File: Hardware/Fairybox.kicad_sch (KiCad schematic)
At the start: 71 parts, among them J1 REED, Q1 SI2302, Q10 C114, Q2 C3200, Q3 C114, Q4 C114, Q5 C3200, Q6 C114, Q7 C114, Q8 C114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

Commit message: Misc changes I forget
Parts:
- removed D8: ORNG, LED_THT:LED_D3.0mm-3, symbol Device:LED_Dual_AAK
- added D22: LED_handsolder, Diode_SMD:D_1206_3216Metric_Pad1.42x1.75mm_HandSolder, symbol Device:LED_Small_Filled
- added D23: LED_nominal, Diode_SMD:D_1206_3216Metric, symbol Device:LED_Small_Filled
- TP1: value GND -> RST
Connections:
- net B- is gone; now on net LI-ION_NEG: BAT1.2 (-), UM1.6 (B-)
- net Q1_BASE: now also R6.2; no longer R6.1
- net REED_RETURN: now also CC3.1, R6.1; no longer R6.2
- net at DI1.2 (A), DI2.2 (A): now also D22.1 (K), D23.1 (K)
- net +BATT renamed CHARGE BOARD OUT B+
- net CHARGE BOARD OUT B+: no longer CC3.1
- net -BATT renamed CHARGE BOARD OUT B-
- net B+ renamed LI-ION_NEG
- net D8_AN1 renamed D22_AN
- net D22_AN: now also D22.2 (A)
- net D8_AN2 renamed D23_AN
- net D23_AN: now also D23.2 (A)
- net RP8 renamed R7_AN
- net SPI RST: no longer names the net of R5.1, TP1.1 (Pin_1), U1.1 (RST)
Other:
- note added: "3.7 LiIon Power Input"
- note added: "5V Power Regulation"
- note added: "ATTiny85 Microcontroller"
- note added: "Ground VIAs"
- note removed: "Vf=1.91"
- moved on the sheet: BAT1, CC3, CC4, CE1, J1, Q1, R5, R6, R7, TP1, TP2, TP3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

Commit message: Misc hardware changes
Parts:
- removed CC3: 2.2nF, Capacitor_THT:C_Disc_D3.0mm_W2.0mm_P2.50mm, symbol Device:C
- removed DI1, DI2: 1N914, Diode_THT:D_DO-35_SOD27_P7.62mm_Horizontal, symbol Diode:1N914
- removed R18, R8: 4.7K, Resistor_THT:R_Axial_DIN0204_L3.6mm_D1.6mm_P5.08mm_Horizontal, symbol Device:R
- removed R19, R9: 47K, Resistor_THT:R_Axial_DIN0204_L3.6mm_D1.6mm_P5.08mm_Horizontal, symbol Device:R
- removed R6: 1K, Resistor_THT:R_Axial_DIN0204_L3.6mm_D1.6mm_P5.08mm_Horizontal, symbol Device:R
- removed R7: 300R, Resistor_THT:R_Axial_DIN0204_L3.6mm_D1.6mm_P5.08mm_Horizontal, symbol Device:R
- added D24, D9: BLUE, Diode_SMD:D_1206_3216Metric, symbol Device:LED_Small_Filled
- added D25: RED, Diode_SMD:D_1206_3216Metric, symbol Device:LED_Small_Filled
- added R16, R8, R9: ??R, Resistor_SMD:R_1206_3216Metric, symbol Device:R_Small
- added R6: 1K, Resistor_SMD:R_1206_3216Metric, symbol Device:R_Small
- CC4: value 0.1uF -> 0.22uF
- D21: renamed from D22; value LED_handsolder -> BLUE
- D23: value LED_nominal -> RED
- Q2, Q5: value C3200 -> C114
- TP10: value TestPoint_Small -> Q8_COL_TP
- TP11: value TestPoint_Small -> Q9_COL_TP
- TP12: value TestPoint_Small -> Q10_COL_TP
- TP6: value TestPoint_Small -> TPP
- TP7: value TestPoint_Small -> Q3_COL TP
- TP8: value TestPoint_Small -> Q2_TP
- TP9: value TestPoint_Small -> Q5_COL TP
- renumbered D21 to D22
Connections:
- net Q2_BASE is gone; now on net MCU GPIO4: Q2.3 (B)
- net Q5_BASE is gone; now on net MCU GPIO3: Q5.3 (B)
- net +5V: now also R16.1, R8.1, R9.1
- net D7_AN: no longer D4.1 (K), D7.2 (A)
- net LI-ION_NEG: no longer BAT1.1 (+), UM1.5 (B+)
- net Q1_BASE: now also R6.2
- net Q2_COL: now also D24.1 (K), D25.1 (K)
- net Q6_COL: now also D9.1 (K)
- net Q7_COL: now also D21.1 (K)
- net Q8_COL: now also D23.1 (K)
- net REED_RETURN: now also R6.1
- net MCU RST: now reaches R5.1, TP1.1 (Pin_1), U1.1 (RST)
- net Q3_COL renamed D6_AN
- new net: D4.1 (K), D7.2 (A)
- new net D24_AN: D24.2 (A), R8.2
- new net D25_AN: D25.2 (A), R16.2
- new net D9_AN: D9.2 (A), R9.2
- new net LI-ION_POS: BAT1.1 (+), UM1.5 (B+)
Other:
- note added: "D6 Vf=3V 5V-3V=2V/0.015A = 133Ω 2V/15Ω = .013A"
- note added: "For oscilloscope spring clips 2"
- note added: "SMD LED"
- note added: "SMD resistor"
- note added: "Test point grounds"
- note removed: "(5-1.91)/470 = 20mA green + 8mA red = orange"
- note removed: "D8 illuminates when either QN9 or QN10 light. The diodes stop D20 and D21 from sinking their current to the transistor collectors opposite of them."
- note removed: "De-ring reed switch"
- note removed: "Poor man's and gate"
- note removed: "Vd=0.461"
- note removed: "Vd=0.462"
- note removed: "Vf=2.05"
- note removed: "Vf=3.06 Ic=0.019A"
- moved on the sheet: CC4, D1, D18, D19, D2, D20, D21, D22, D23, D3, D4, D5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

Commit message: Updated testpoints and silkscreen
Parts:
- JP2, JP4, JP6, JP7, JP8: footprint UltraLibrary:Via-GND -> UltraLibrary:PTH-Test_Point; symbol ultra_library:ViaGND -> ultra_library:PTH-TestPoint_to_GND
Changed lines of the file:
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@@
     (effects (font (size 1 1)) (justify left bottom))
   )
-  (symbol (lib_id "ultra_library:ViaGND") (at 256.54 250.825 0) (unit 1)
+  (symbol (lib_id "ultra_library:PTH-TestPoint_to_GND") (at 256.54 250.825 0) (unit 1)
     (in_bom yes) (on_board yes)
     (property "Reference" "JP7" (id 0) (at 254 248.285 0)
@@
       (effects (font (size 1.27 1.27)) (justify left) hide)
     )
-    (property "Footprint" "UltraLibrary:Via-GND" (id 2) (at 256.54 250.825 0)
+    (property "Footprint" "UltraLibrary:PTH-Test_Point" (id 2) (at 256.54 250.825 0)
       (effects (font (size 1.27 1.27)) hide)
     )
@@
     (pin "2")
   )
-  (symbol (lib_id "ultra_library:ViaGND") (at 251.46 250.825 0) (unit 1)
+  (symbol (lib_id "ultra_library:PTH-TestPoint_to_GND") (at 251.46 250.825 0) (unit 1)
     (in_bom yes) (on_board yes)
     (property "Reference" "JP8" (id 0) (at 248.92 248.285 0)
@@
       (effects (font (size 1.27 1.27)) (justify left) hide)
     )
-    (property "Footprint" "UltraLibrary:Via-GND" (id 2) (at 251.46 250.825 0)
+    (property "Footprint" "UltraLibrary:PTH-Test_Point" (id 2) (at 251.46 250.825 0)
       (effects (font (size 1.27 1.27)) hide)
     )
@@
     (pin "1")
   )
-  (symbol (lib_id "ultra_library:ViaGND") (at 245.11 250.825 0) (unit 1)
+  (symbol (lib_id "ultra_library:PTH-TestPoint_to_GND") (at 245.11 250.825 0) (unit 1)
     (in_bom yes) (on_board yes)
     (property "Reference" "JP6" (id 0) (at 242.57 248.285 0)
@@
       (effects (font (size 1.27 1.27)) (justify left) hide)
     )
-    (property "Footprint" "UltraLibrary:Via-GND" (id 2) (at 245.11 250.825 0)
+    (property "Footprint" "UltraLibrary:PTH-Test_Point" (id 2) (at 245.11 250.825 0)
       (effects (font (size 1.27 1.27)) hide)
     )
@@
     (pin "2")
   )
-  (symbol (lib_id "ultra_library:ViaGND") (at 262.255 250.825 0) (unit 1)
+  (symbol (lib_id "ultra_library:PTH-TestPoint_to_GND") (at 262.255 250.825 0) (unit 1)
     (in_bom yes) (on_board yes)
     (property "Reference" "JP4" (id 0) (at 259.715 248.285 0)
@@
       (effects (font (size 1.27 1.27)) (justify left) hide)
     )
-    (property "Footprint" "UltraLibrary:Via-GND" (id 2) (at 262.255 250.825 0)
+    (property "Footprint" "UltraLibrary:PTH-Test_Point" (id 2) (at 262.255 250.825 0)
       (effects (font (size 1.27 1.27)) hide)
     )
@@
     (pin "1")
   )
-  (symbol (lib_id "ultra_library:ViaGND") (at 239.395 250.825 0) (unit 1)
+  (symbol (lib_id "ultra_library:PTH-TestPoint_to_GND") (at 239.395 250.825 0) (unit 1)
     (in_bom yes) (on_board yes)
     (property "Reference" "JP2" (id 0) (at 236.855 248.285 0)
@@
       (effects (font (size 1.27 1.27)) (justify left) hide)
     )
-    (property "Footprint" "UltraLibrary:Via-GND" (id 2) (at 239.395 250.825 0)
+    (property "Footprint" "UltraLibrary:PTH-Test_Point" (id 2) (at 239.395 250.825 0)
       (effects (font (size 1.27 1.27)) hide)
     )
@@
     )
     (path "/d32c4ef7-dff3-42ca-b263-850b4f362096"
-      (reference "JP2") (unit 1) (value "ViaGND") (footprint "UltraLibrary:Via-GND")
+      (reference "JP2") (unit 1) (value "ViaGND") (footprint "UltraLibrary:PTH-Test_Point")
     )
     (path "/5a3db8f0-f842-4403-92aa-21d7fe3462d6"
@@
     )
     (path "/cfccbb7b-ccad-4118-94a3-53227b3d839f"
-      (reference "JP4") (unit 1) (value "ViaGND") (footprint "UltraLibrary:Via-GND")
+      (reference "JP4") (unit 1) (value "ViaGND") (footprint "UltraLibrary:PTH-Test_Point")
     )
     (path "/73116c89-7ad9-480c-9a9b-9373298241f3"
@@
     )
     (path "/4da5f2d2-051f-4fbb-b355-53557e1b2b87"
-      (reference "JP6") (unit 1) (value "ViaGND") (footprint "UltraLibrary:Via-GND")
+      (reference "JP6") (unit 1) (value "ViaGND") (footprint "UltraLibrary:PTH-Test_Point")
     )
     (path "/02ec95bc-9b18-4028-a83d-b583d5fdd405"
-      (reference "JP7") (unit 1) (value "ViaGND") (footprint "UltraLibrary:Via-GND")
+      (reference "JP7") (unit 1) (value "ViaGND") (footprint "UltraLibrary:PTH-Test_Point")
     )
     (path "/111b3249-5eff-4101-9c94-370558af5ec1"
-      (reference "JP8") (unit 1) (value "ViaGND") (footprint "UltraLibrary:Via-GND")
+      (reference "JP8") (unit 1) (value "ViaGND") (footprint "UltraLibrary:PTH-Test_Point")
     )
     (path "/36b807a0-a817-4a09-a5f8-3ee2792c5a71"

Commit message: misc
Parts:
- added D?: D_Schottky, symbol Device:D_Schottky
- added R?: 22R, Resistor_THT:R_Axial_DIN0204_L3.6mm_D1.6mm_P5.08mm_Horizontal, symbol Device:R
- added R? (x5): 250R, Resistor_THT:R_Axial_DIN0204_L3.6mm_D1.6mm_P5.08mm_Horizontal, symbol Device:R
- R16: value ??R -> 170R
- R8: value ??R -> 470R
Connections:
- net +5V: now also D?.2 (A); no longer CC4.1, TP5.1 (Pin_1), U1.8 (VCC)
- net MCU GPIO0 MOSI: now also R?.2
- net MCU GPIO1 MISO: now also R?.2
- net MCU GPIO2 SCK: now also R?.2
- net MCU GPIO3: now also R?.2
- net MCU GPIO4: now also R?.2
- new net: R?.2, TP5.1 (Pin_1)
- new net: CC4.1, R?.1, U1.8 (VCC)
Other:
- note added: "1/8W Current limiting resistors GPIO Imax=20mA 4.5V/0.020A = 0.018A Also protects ISP programmer"
- note added: "1W current limiting resistor 5V/22 = 0.230A Also prevents ISP from powering LEDs."
- note added: "BLUE"
- note added: "RED"
- moved on the sheet: D3, D4, D7, Q4, Q5, R3, R4, TP5, TP6, TP9

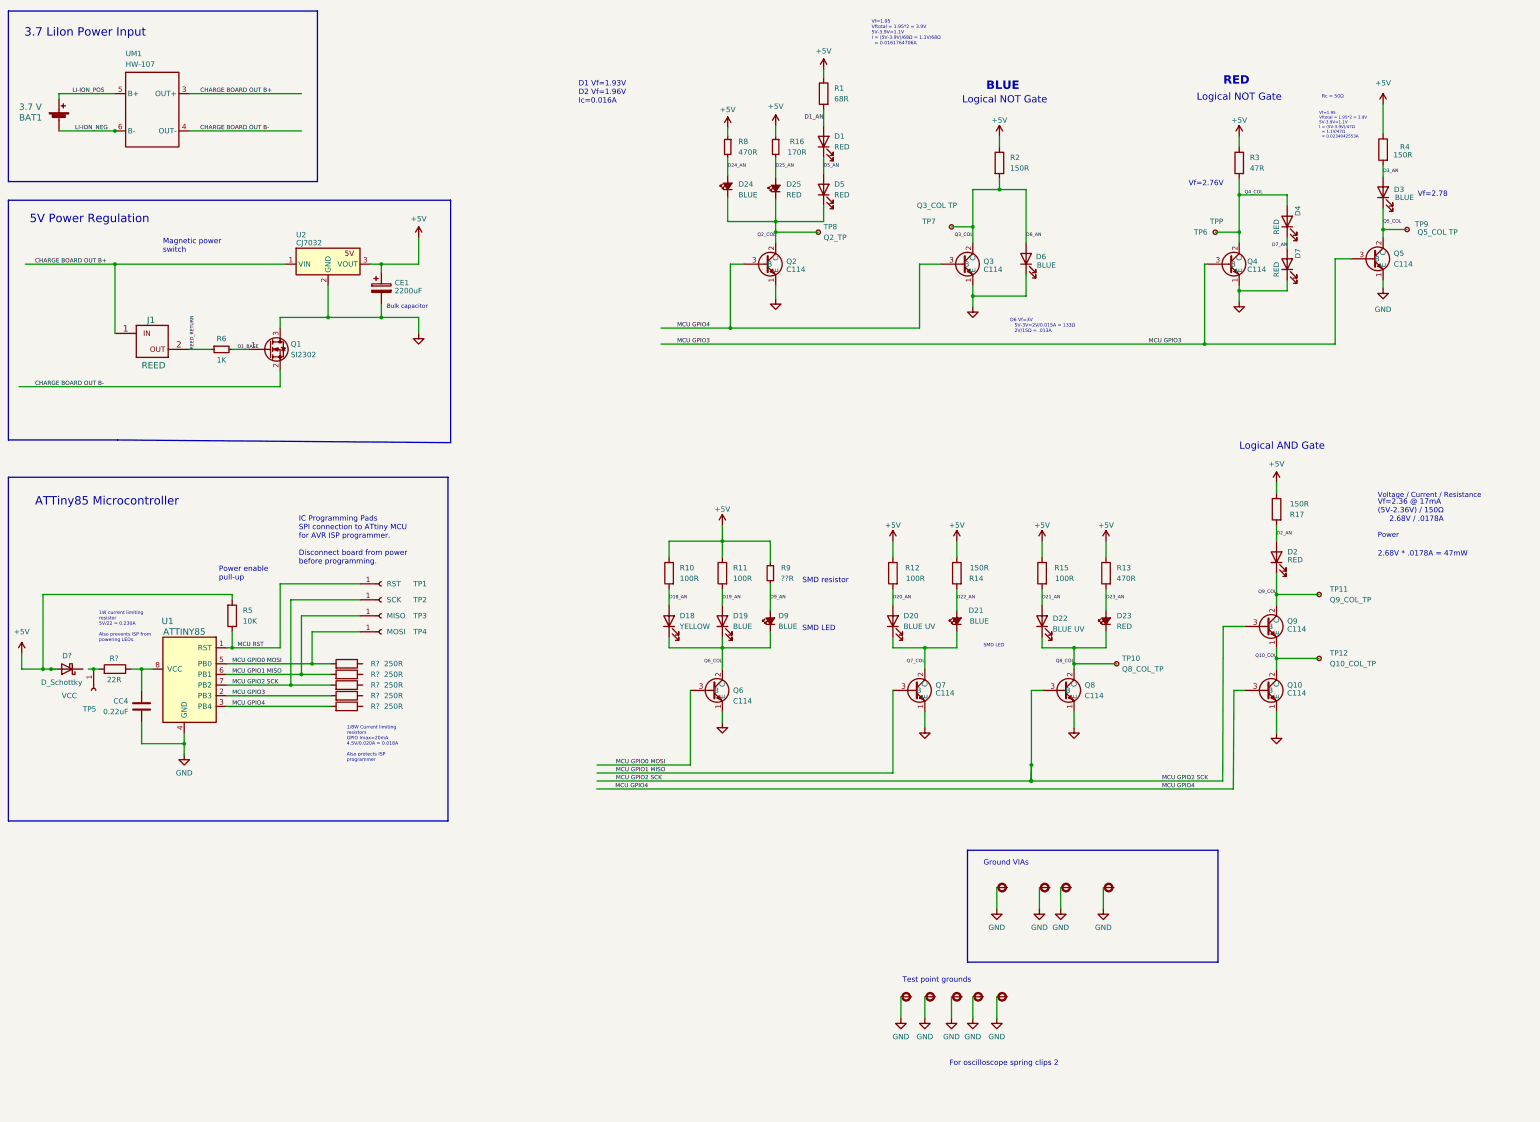
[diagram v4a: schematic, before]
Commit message: Power Delivery  EEschema   - Added two 1x2P 2.5mm pitch pin header symbols with associated footprints to replace the custom liion charge breakout board symbol/footprints   - Moved liion charge board and n-channel mosfet south on the board to make room for:   - Shifted 18650 battery sled from the right of the board to the center, allowing room for some SMD leds around the board periphery.  PCBnew   - New lion charge board pin headers
MCU
 EEschema
  - Added 220R series resistors (R7, R18, R19) to each MCU pin used for SPI in circuit programming. Protects the programmer GPIO pins from voltages greater than 22mA
 PCBnew
  - 220R series resistors added to SPI lines at the bottom of the board. Shifted tracks around a little to get them to fit. The resistors will be under the exclusion zone, but they're small so it's okay.

Lighting
 PCBnew
  - Rotated LED D4 so the leads can be bent without running into it's neighbour
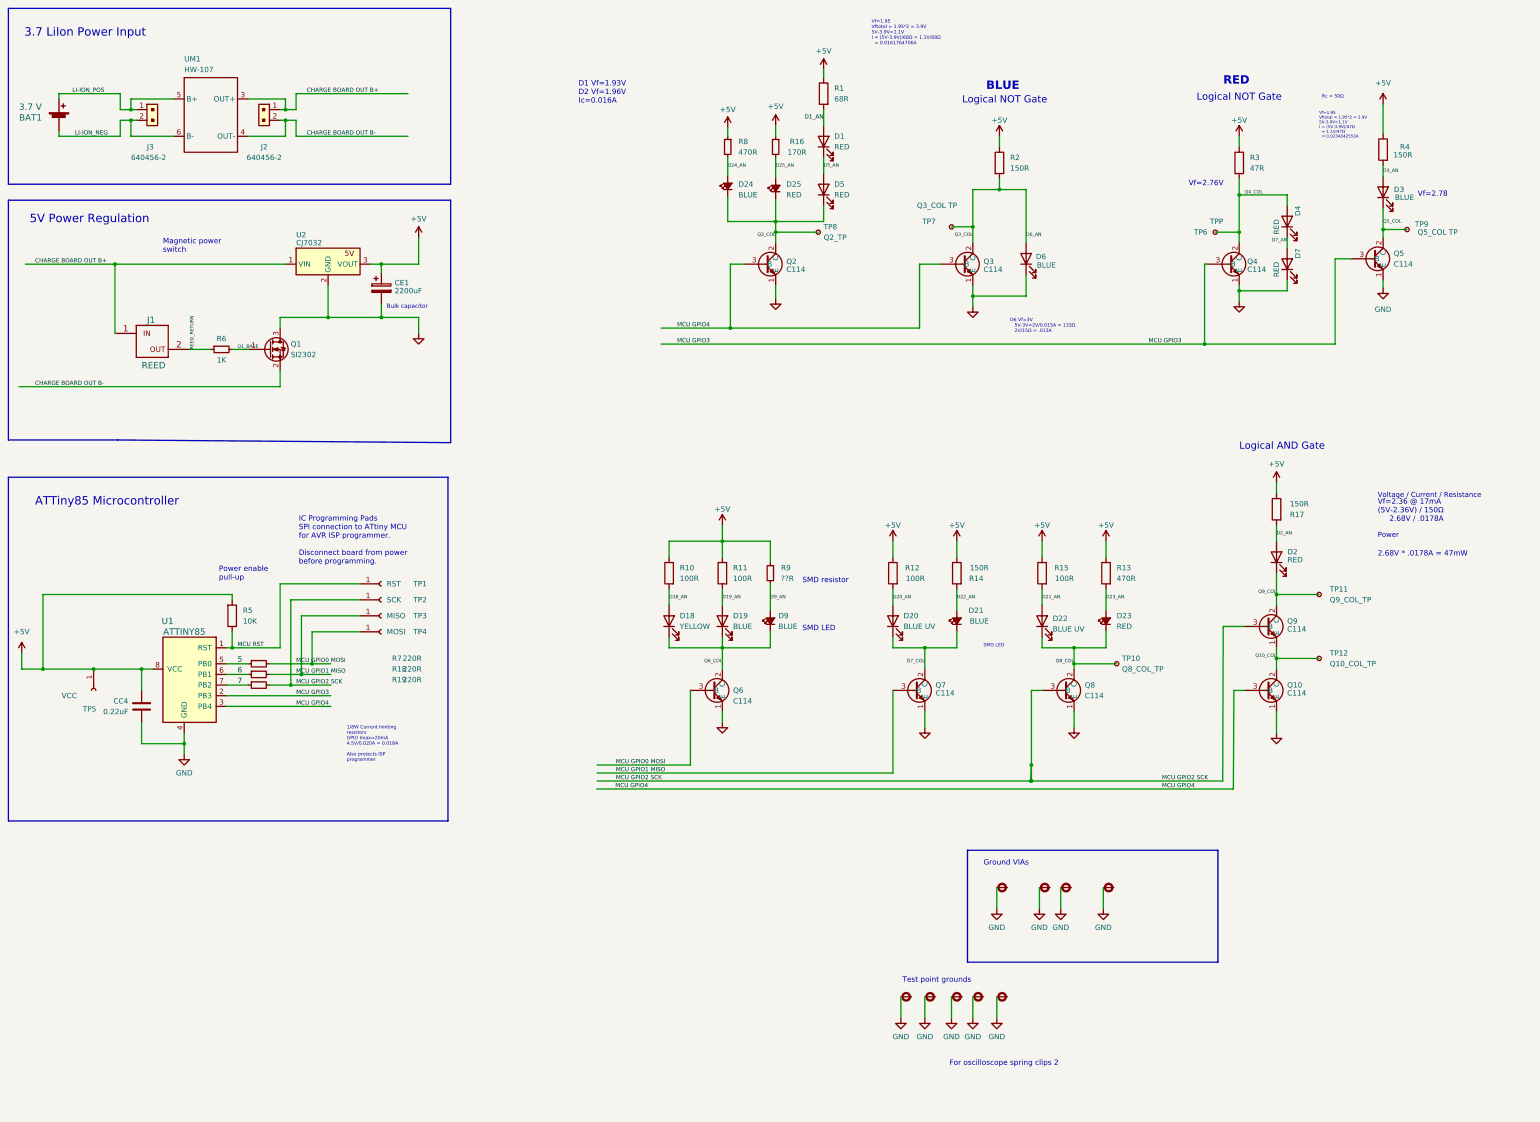
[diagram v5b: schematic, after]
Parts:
- removed D?: D_Schottky, symbol Device:D_Schottky
- removed R?: 22R, Resistor_THT:R_Axial_DIN0204_L3.6mm_D1.6mm_P5.08mm_Horizontal, symbol Device:R
- removed R? (x5): 250R, Resistor_THT:R_Axial_DIN0204_L3.6mm_D1.6mm_P5.08mm_Horizontal, symbol Device:R
- added J2, J3: 640456-2, digikey-footprints:PinHeader_1x2_P2.54mm, symbol dk_Rectangular-Connectors-Headers-Male-Pins:640456-2
- added R18, R19, R7: 220R, Resistor_SMD:R_1206_3216Metric, symbol Device:R_Small
- UM1: now left out of the parts list
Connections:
- net +5V: now also CC4.1, TP5.1 (Pin_1), U1.8 (VCC)
- net CHARGE BOARD OUT B+: now also J2.1
- net CHARGE BOARD OUT B-: now also J2.2
- net D7_AN: now also D4.1 (K), D7.2 (A)
- net LI-ION_NEG: now also J3.2
- net LI-ION_POS: now also J3.1
- net MCU GPIO0 MOSI: now also R7.2; no longer U1.5 (PB0)
- net MCU GPIO1 MISO: now also R18.2; no longer U1.6 (PB1)
- net MCU GPIO2 SCK: now also R19.2; no longer U1.7 (PB2)
- new net 5: R7.1, U1.5 (PB0)
- new net 6: R18.1, U1.6 (PB1)
- new net 7: R19.1, U1.7 (PB2)
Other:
- note removed: "1W current limiting resistor 5V/22 = 0.230A Also prevents ISP from powering LEDs."
- moved on the sheet: UM1

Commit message: JST connector, Rule Zone Added JST PH connector instead of screw terminals. Corrected keepout zone.
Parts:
- removed J2, J3: 640456-2, digikey-footprints:PinHeader_1x2_P2.54mm, symbol dk_Rectangular-Connectors-Headers-Male-Pins:640456-2
- added J2: JST B4B-PH-K-S, Connector_JST:JST_PH_B4B-PH-K_1x04_P2.00mm_Vertical, symbol Connector_Generic_MountingPin:Conn_01x04_MountingPin
- Q6, Q7: value C114 -> C144
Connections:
- net 5: now also TP4.1 (Pin_1)
- net 6: now also TP3.1 (Pin_1)
- net 7: now also TP2.1 (Pin_1)
- net CHARGE BOARD OUT B+: now also J2.4 (Pin_4)
- net CHARGE BOARD OUT B-: now also J2.3 (Pin_3)
- net LI-ION_NEG: now also J2.2 (Pin_2)
- net LI-ION_POS: now also J2.1 (Pin_1)
- net MCU GPIO0 MOSI: no longer TP4.1 (Pin_1)
- net MCU GPIO1 MISO: no longer TP3.1 (Pin_1)
- net MCU GPIO2 SCK: no longer TP2.1 (Pin_1)
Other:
- moved on the sheet: BAT1, R18, R19, R7, TP5, UM1

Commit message: many
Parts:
- added Q14: AO3401A, Package_TO_SOT_SMD:SOT-23, symbol Transistor_FET:AO3401A
- added Q15, Q16: SI2302, Package_TO_SOT_SMD:SOT-23, symbol Transistor_FET:TSM2302CX
- added R20: 100K, Resistor_SMD:R_1206_3216Metric, symbol Device:R_Small
- added R22: 1M, Resistor_SMD:R_1206_3216Metric, symbol Device:R_Small
- added R23: 330k, Resistor_SMD:R_1206_3216Metric, symbol Device:R_Small
- R18, R19, R7: value 220R -> 470R
- R6: value 1K -> 10K
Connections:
- net +5V: now also Q14.2 (S), Q15.3 (D); no longer R10.1, R11.1, R14.1, R15.1, R2.1, R4.1, R8.1, R9.1
- net CHARGE BOARD OUT B-: now also R20.1
- net GND: now also Q16.2 (S), R23.1
- net LI-ION_POS: now also R22.2
- net Q1_BASE renamed Q1_GATE
- net Q1_GATE: now also R20.2
- new net: Q14.1 (G), Q16.1 (G), R22.1, R23.2
- new net: Q14.3 (D), Q15.1 (G), Q16.3 (D)
- new net +5V B-LED: Q15.2 (S), R14.1, R15.1, R2.1, R4.1, R8.1, R9.1
- new net BLUE LED RESISTOR ANODES: R10.1, R11.1
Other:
- note added: "3V = 0.528V"
- note added: "Gate closes at low V"
- note added: "ISP Programmer Protection Limiting shared SPI lines to 10mA to protect leds from damaging AVR ISP GPIO. 5V/0.010A = 500Ω ideal resistance. 5V/470Ω = 0.011A"
- note added: "NOT gate"
- note added: "P-channel"
- note added: "Scenario 1"
- note added: "VBATT = 3.5V"
- note added: "When VCC < 3V, Vg > 0.5V +5V to Blue LED resistor + off"
- moved on the sheet: R6, TP5

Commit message: a lot
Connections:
- net BLUE LED RESISTOR ANODES is gone; now on net +5V B-LED: R10.1, R11.1
- net +5V: now also R8.1
- net +5V B-LED: no longer R8.1
- net CHARGE BOARD OUT B+: now also R6.2; no longer J1.1
- net Q1_GATE: now also J1.2; no longer R6.2
- net LBAT_NOT: now reaches Q14.1 (G), Q16.1 (G), R22.1, R23.2
- net Q15_COL: now reaches Q14.3 (D), Q15.1 (G), Q16.3 (D)
- net 5 renamed PB0 PHY
- net 6 renamed PB1 PHY
- net 7 renamed PB2 PHY
- net REED_RETURN renamed REED_IN
- net REED_IN: now also J1.1; no longer J1.2
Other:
- note added: "ESP8266 AVR ISP GPIO protection 1/8W Current limiting resistors GPIO Imax=12mA 5V/0.012A = 417Ω 5V/470R = 10mA"
- note added: "Programming Pads SPI connection to ATtiny MCU for AVR ISP programmer."
- note added: "Supplement internal RESET pull-up"
- note removed: "1/8W Current limiting resistors GPIO Imax=20mA 4.5V/0.020A = 0.018A Also protects ISP programmer"
- note removed: "IC Programming Pads SPI connection to ATtiny MCU for AVR ISP programmer. Disconnect board from power before programming."
- note removed: "ISP Programmer Protection Limiting shared SPI lines to 10mA to protect leds from damaging AVR ISP GPIO. 5V/0.010A = 500Ω ideal resistance. 5V/470Ω = 0.011A"
- note removed: "Power enable pull-up"
- moved on the sheet: Q15, R18, R19, R6, R7, TP1
